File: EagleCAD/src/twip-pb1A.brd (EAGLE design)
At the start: 100 x 48.2 mm, 22 parts, among them J1 UJ2-BH-1-TH

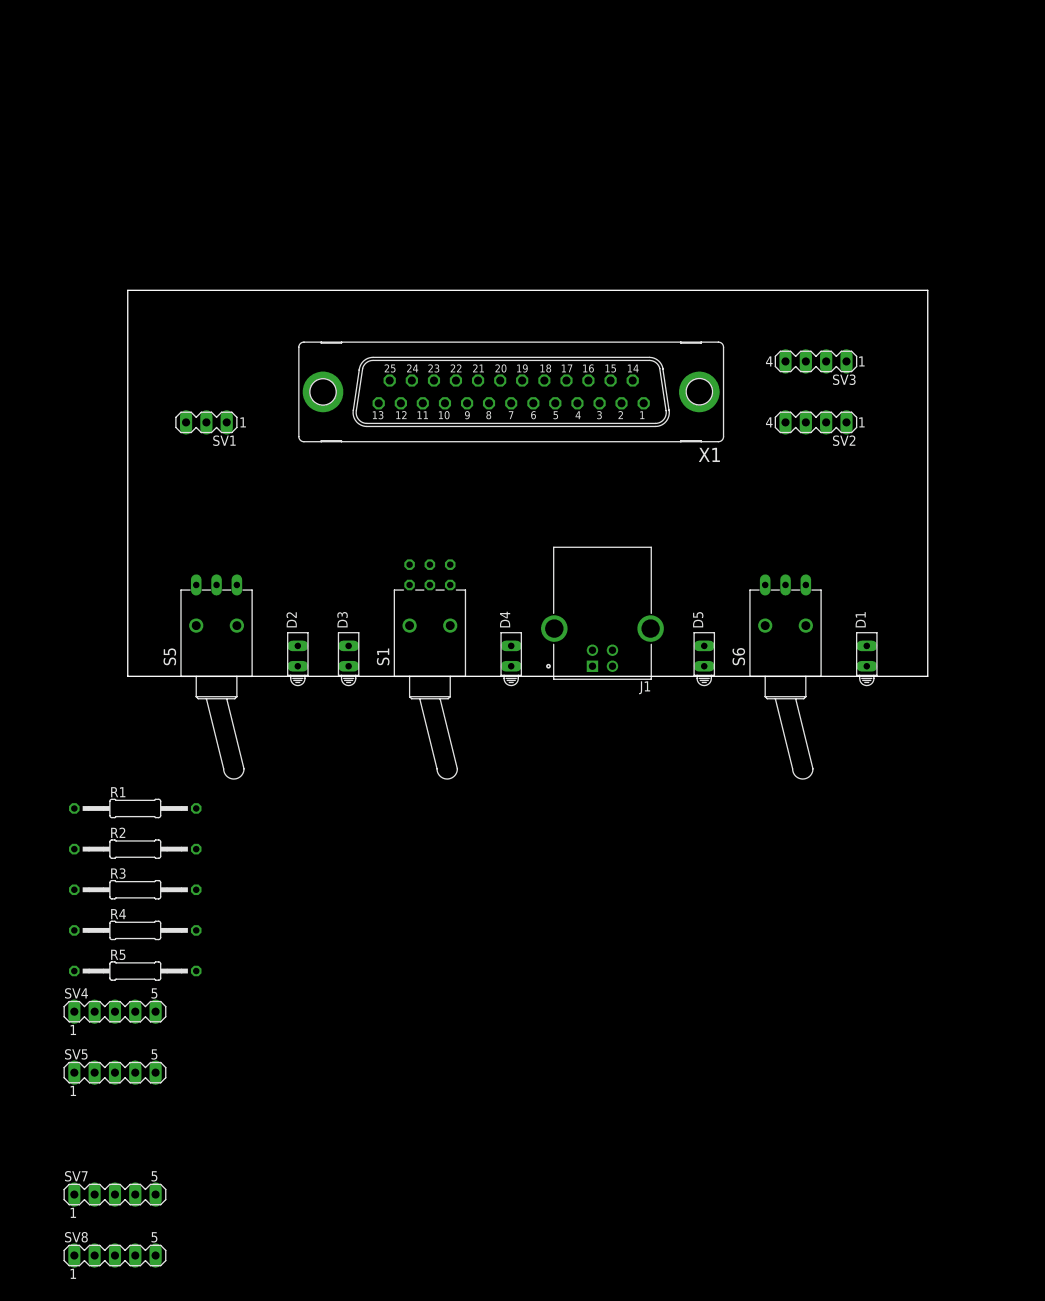
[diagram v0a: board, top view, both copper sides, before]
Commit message: Sep 24 checkpoint has mutually consistent versions of MB and PB layouts, and pinouts documentation
completed layout of peripheral board, with a few retrofits to MB for IBC connector changes. Added a 4 position DIP switch to PB as a way to have jumpers that cross other traces, as I couldn't quite do a single sided layout. All switches go to the right when active, and the voltage regulators, whose 4 legs are represented by two 5 pin headers, are correctly scaled. I'd like to space out the top connector for the stepper motor connections, but the board is at the max size allowed, and Eagle CAD won't allow it to be moved upward.
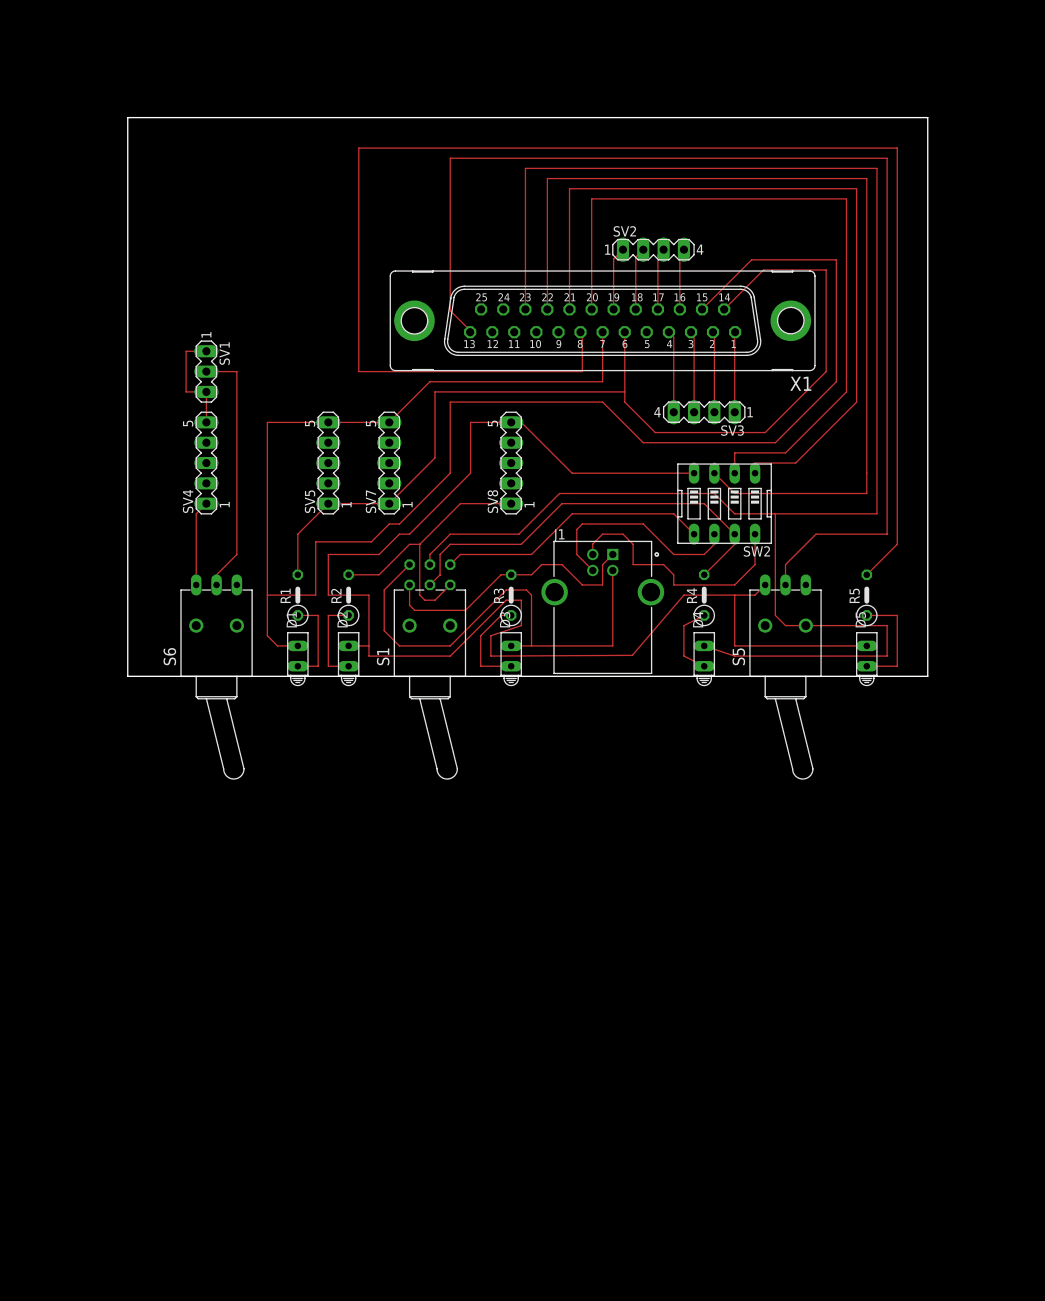
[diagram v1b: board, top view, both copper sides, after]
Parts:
- added SW2: (no value), special:EDG-04
- R1, R2, R3, R4, R5: device resistor:0207/15 -> resistor:0207/5V
- moved SV8 110.8 mm to (49.5, 58.4), turned to 90 degrees
- moved R5 102.8 mm to (94.0, 41.9), turned to 90 degrees
- moved SV7 97.7 mm to (34.3, 58.4), turned to 90 degrees
- moved R4 82.5 mm to (73.7, 41.9), turned to 90 degrees
- moved SV5 80.7 mm to (26.7, 58.4), turned to 90 degrees
- moved D1 71.1 mm to (22.9, 34.3)
- moved S5 71.1 mm to (83.8, 38.1)
- moved S6 71.1 mm to (12.7, 38.1)
- moved SV4 69.5 mm to (11.4, 58.4), turned to 90 degrees
- moved R3 59.7 mm to (49.5, 41.9), turned to 90 degrees
- moved R2 41.5 mm to (29.2, 41.9), turned to 90 degrees
- moved R1 33.5 mm to (22.9, 41.9), turned to 90 degrees
- moved SV2 29.6 mm to (67.3, 85.1), turned to 0 degrees
- moved D4 24.1 mm to (73.7, 34.3)
- moved D5 20.3 mm to (94.0, 34.3)
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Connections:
- new net N$22: R4.2, S1.2, SW2.7
- new net N$23: D3.K, J1.4, S1.6
- new net N$24: SW2.1, X1.21
- new net N$25: SW2.3, X1.22
- new net N$26: SW2.2, X1.20
- new net N$27: D4.K, S1.5, X1.23
- new net N$28: S5.2, X1.13
- new net N$29: D1.K, SV5.5, SV7.5, X1.15, X1.7
- new net N$30: S1.4, SW2.5
- new net N$31: D2.K, D5.K, S5.3, SV8.5, SW2.4
- new net N$33: J1.3, SW2.6
- net N$1: now also D1.A; no longer D2.A
- net N$10: now also S6.3; no longer S6.2
- net N$12: now also S1.1
- net N$13: now also J1.2, SW2.8; no longer D1.K, SV8.5
- net N$2: now also D2.A; no longer D1.A
- net N$7: now also S6.2; no longer S6.3
- net N$8: now also X1.14
- net N$9: now also J1.1, R3.2, S1.3; no longer D2.K, SV5.5, SV7.5, X1.5
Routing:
- net N$27: track 0.00 -> 220.2 mm
- net N$29: track 0.00 -> 211.3 mm
- net N$21: track 0.00 -> 183.1 mm
- net N$31: track 0.00 -> 172.0 mm
- net N$28: track 0.00 -> 141.2 mm
- net N$8: track 0.00 -> 124.3 mm
- net N$25: track 0.00 -> 115.8 mm
- net N$24: track 0.00 -> 94.8 mm
- net N$26: track 0.00 -> 89.7 mm
- net N$23: track 0.00 -> 60.4 mm
- net N$22: track 0.00 -> 52.1 mm
- net N$12: track 0.00 -> 35.2 mm
- net N$9: track 0.00 -> 34.7 mm
- net N$30: track 0.00 -> 34.2 mm
- net N$13: track 0.00 -> 31.8 mm
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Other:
- board size 100 x 48.2 mm -> 100 x 69.8 mm

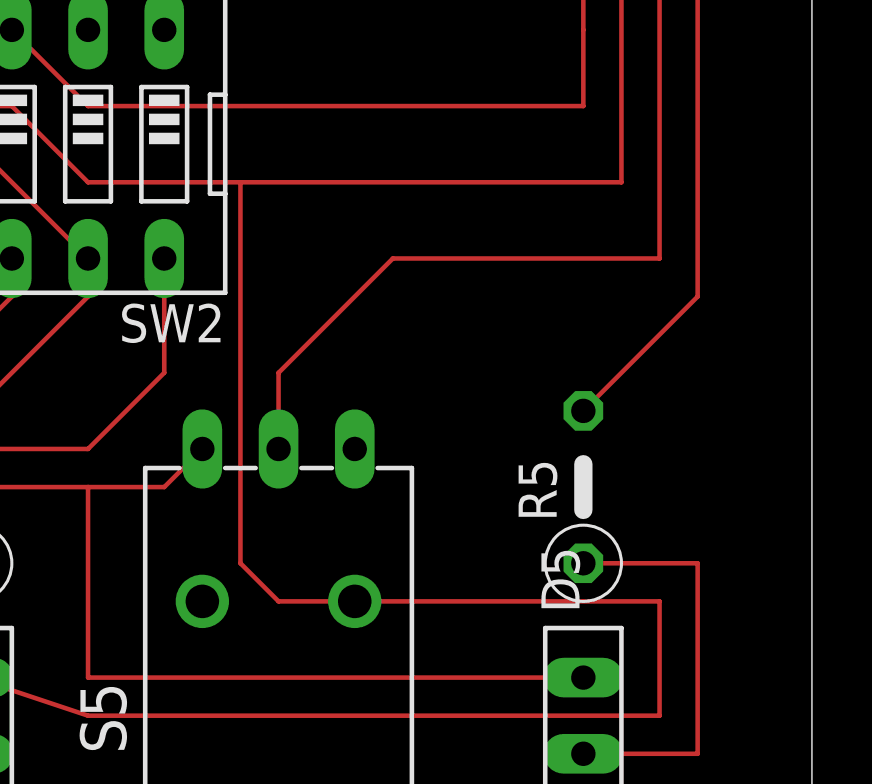
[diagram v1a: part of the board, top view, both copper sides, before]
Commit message: minor layout fixes
need to use version numbers built into copper plate.
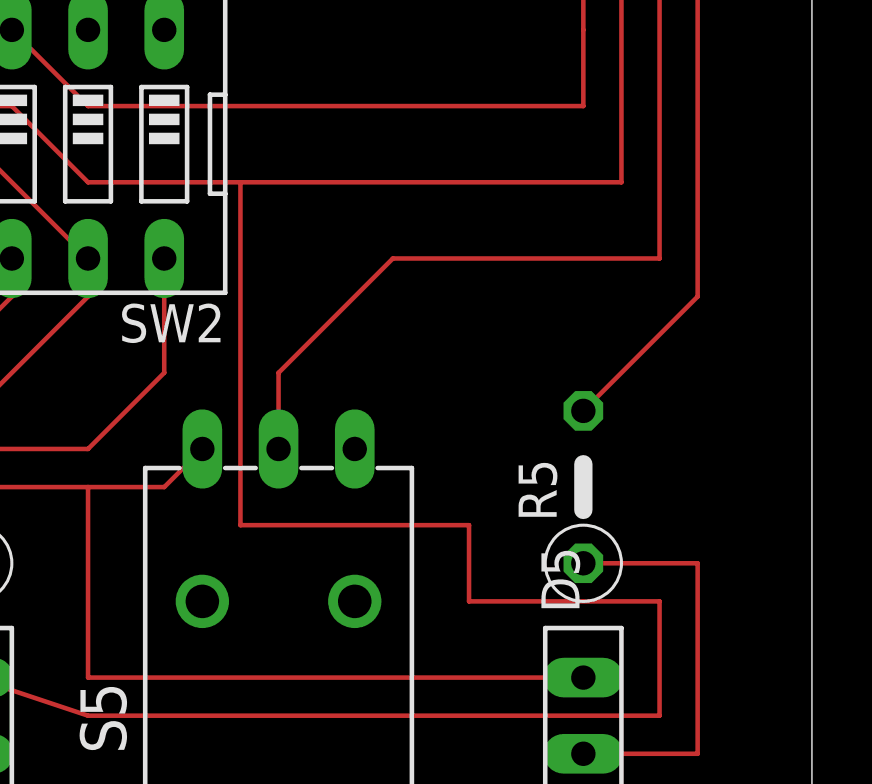
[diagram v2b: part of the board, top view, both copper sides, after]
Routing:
- net N$27: track 220.2 -> 220.9 mm
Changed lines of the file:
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@@
 <contactref element="D4" pad="K"/>
 <wire x1="55.5752" y1="54.61" x2="50.4952" y2="49.53" width="0.1524" layer="1"/>
-<wire x1="83.82" y1="38.1" x2="96.52" y2="38.1" width="0.1524" layer="1"/>
 <wire x1="96.52" y1="38.1" x2="96.52" y2="34.29" width="0.1524" layer="1"/>
 <wire x1="96.52" y1="34.29" x2="77.47" y2="34.29" width="0.1524" layer="1"/>
@@
 <wire x1="39.37" y1="45.72" x2="39.37" y2="46.99" width="0.1524" layer="1"/>
 <wire x1="41.91" y1="49.53" x2="50.4952" y2="49.53" width="0.1524" layer="1"/>
-<wire x1="82.55" y1="39.37" x2="83.82" y2="38.1" width="0.1524" layer="1"/>
 <wire x1="51.308" y1="95.25" x2="95.25" y2="95.25" width="0.1524" layer="1"/>
 <wire x1="95.25" y1="95.25" x2="95.25" y2="52.07" width="0.1524" layer="1"/>
@@
 <wire x1="77.47" y1="52.07" x2="74.93" y2="54.61" width="0.1524" layer="1"/>
 <wire x1="74.93" y1="54.61" x2="55.5752" y2="54.61" width="0.1524" layer="1"/>
-<wire x1="82.55" y1="39.37" x2="82.55" y2="52.07" width="0.1524" layer="1"/>
+<wire x1="82.55" y1="40.64" x2="82.55" y2="52.07" width="0.1524" layer="1"/>
 <wire x1="39.37" y1="46.99" x2="41.91" y2="49.53" width="0.1524" layer="1"/>
+<wire x1="82.55" y1="40.64" x2="90.17" y2="40.64" width="0.1524" layer="1"/>
+<wire x1="90.17" y1="40.64" x2="90.17" y2="38.1" width="0.1524" layer="1"/>
+<wire x1="90.17" y1="38.1" x2="96.52" y2="38.1" width="0.1524" layer="1"/>
 </signal>
 <signal name="N$28">

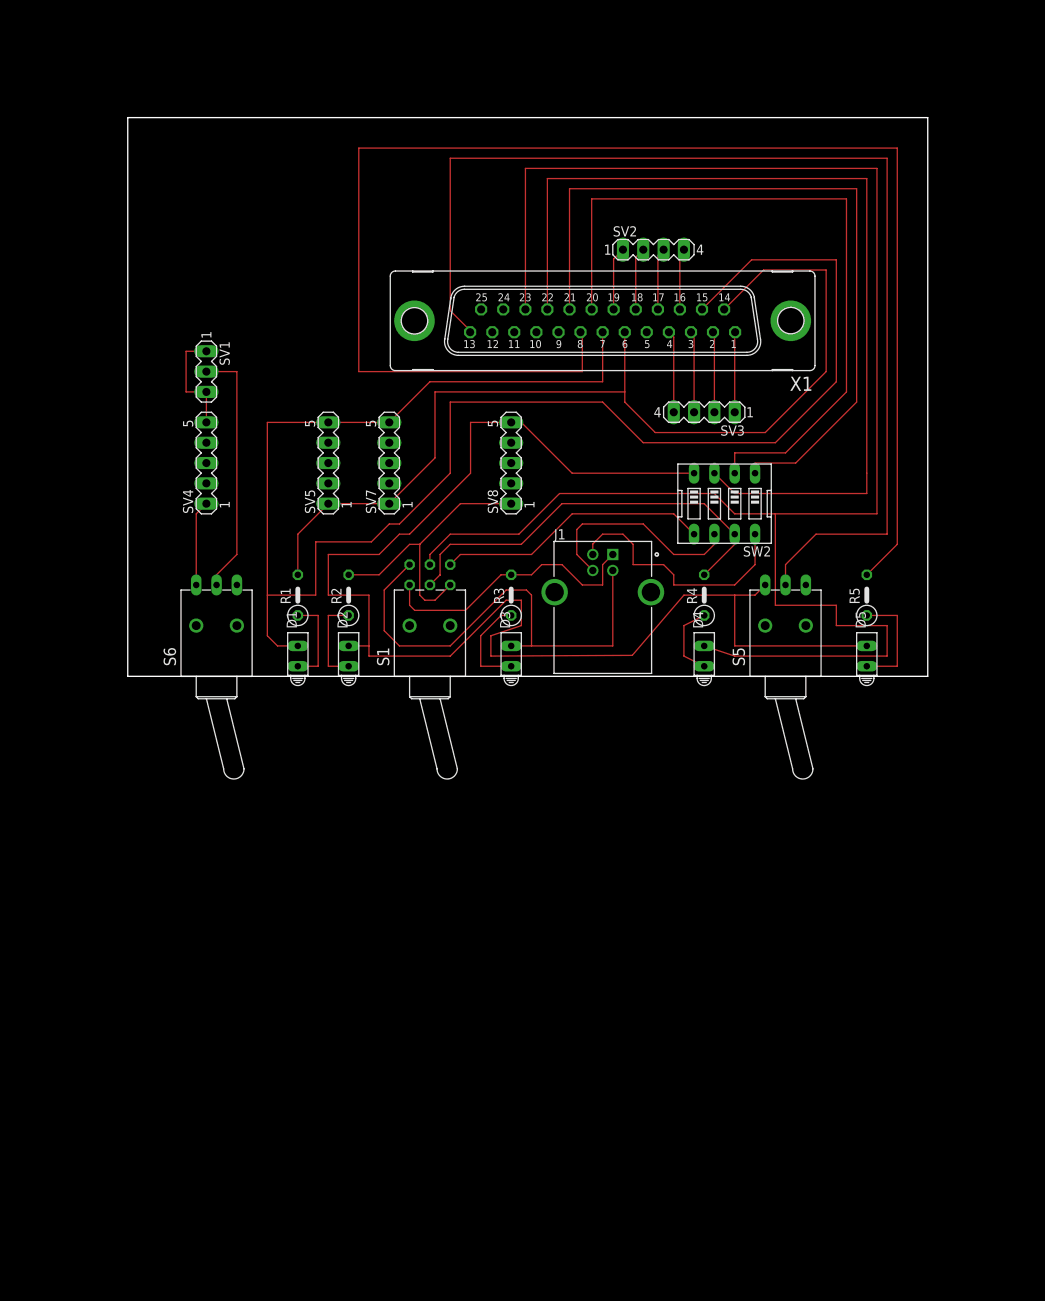
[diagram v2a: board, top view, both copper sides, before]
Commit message: minor fixes, and upsized boards to 3.3 x 5 inches
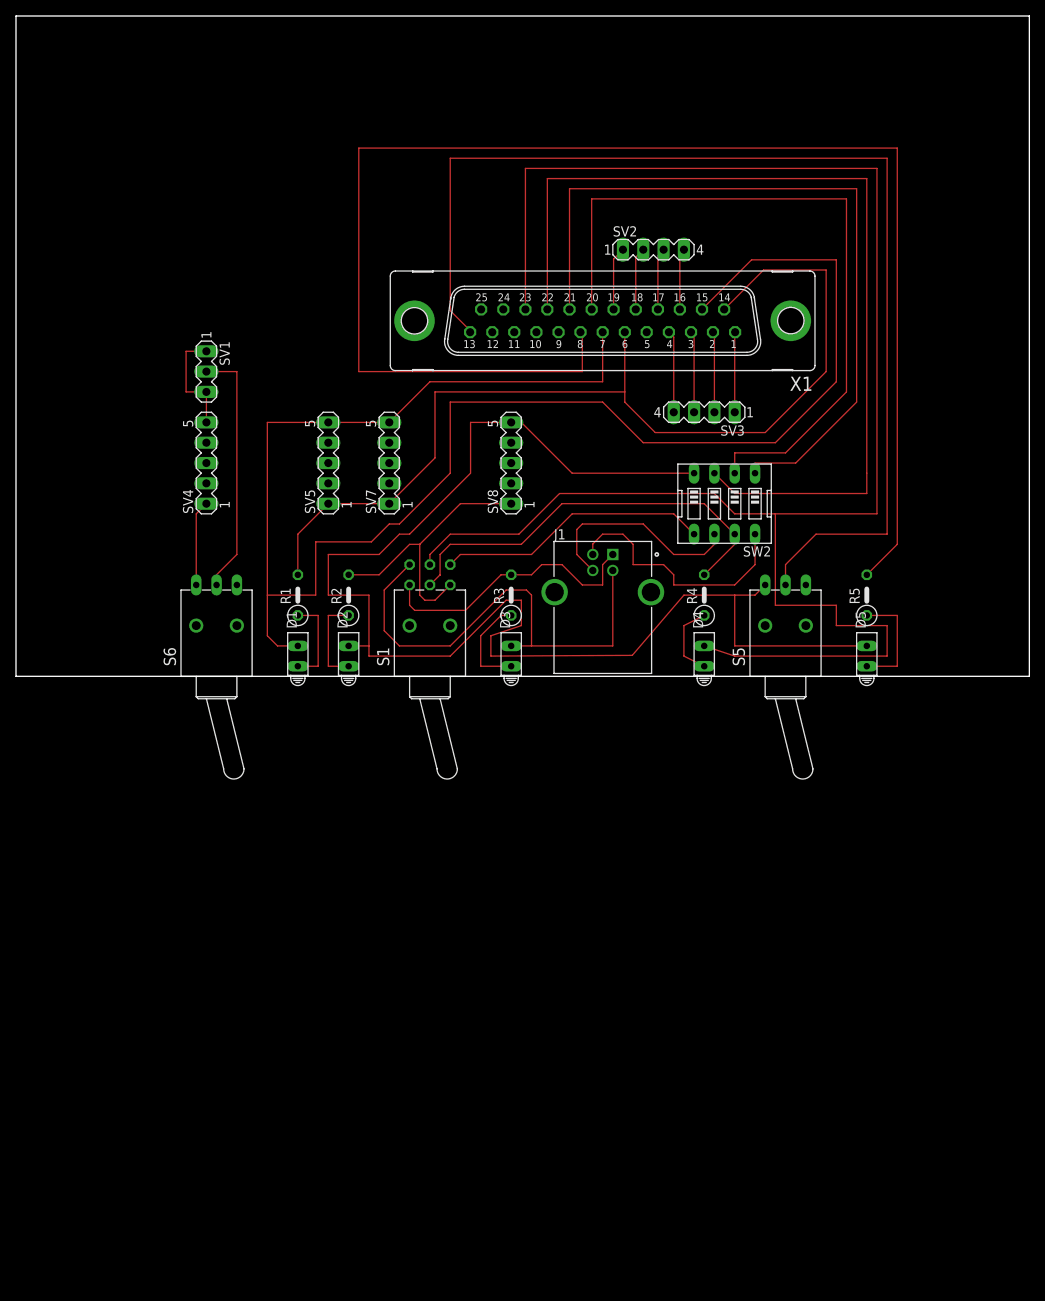
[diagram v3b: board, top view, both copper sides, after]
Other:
- board size 100 x 69.8 mm -> 126.7 x 82.5 mm
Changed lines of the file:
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@@
 <setting verticaltext="up"/>
 </settings>
-<grid distance="50" unitdist="mil" unit="mil" style="lines" multiple="1" display="no" altdistance="5" altunitdist="mil" altunit="mil"/>
+<grid distance="50" unitdist="mil" unit="mil" style="lines" multiple="10" display="yes" altdistance="5" altunitdist="mil" altunit="mil"/>
 <layers>
 <layer number="1" name="Top" color="4" fill="1" visible="yes" active="yes"/>
@@
 </layers>
 <board>
+<fusionsync huburn="a.cGVyc29uYWw6dWUyZDlmNmRl" projecturn="a.cGVyc29uYWw6dWUyZDlkNTAxIzIwMTgwODE4MTQ0NTE2MDUx" f3durn="urn:adsk.wipprod:dm.lineage:0yhwyiUNTZiQcmkfIzc17A" pcbguid="0e7eb315-b537-445a-a3fe-deb230e75ce0" lastpulledtime="" lastsyncedchangeguid="4e02391e-1938-e666-ed35-ac1e4dc4cf74"/>
 <plain>
-<wire x1="101.6" y1="101.6" x2="1.6" y2="101.6" width="0" layer="20"/>
-<wire x1="1.6" y1="101.6" x2="1.6" y2="31.76" width="0" layer="20"/>
-<wire x1="1.6" y1="31.76" x2="101.6" y2="31.76" width="0" layer="20"/>
-<wire x1="101.6" y1="31.76" x2="101.6" y2="101.6" width="0" layer="20"/>
-<dimension x1="101.6" y1="26.67" x2="2.54" y2="24.13" x3="52.07" y3="25.4" textsize="1.778" layer="1" dtype="horizontal" unit="inch"/>
-<dimension x1="-1.27" y1="31.75" x2="-1.27" y2="80.01" x3="-2.54" y3="55.88" textsize="1.778" layer="1" dtype="horizontal" unit="inch"/>
+<wire x1="114.3" y1="114.3" x2="-12.37" y2="114.3" width="0" layer="20"/>
+<wire x1="-12.37" y1="114.3" x2="-12.37" y2="31.76" width="0" layer="20"/>
+<wire x1="-12.37" y1="31.76" x2="114.3" y2="31.76" width="0" layer="20"/>
+<wire x1="114.3" y1="31.76" x2="114.3" y2="114.3" width="0" layer="20"/>
+<dimension x1="114.3" y1="120.65" x2="-12.7" y2="120.65" x3="50.8" y3="123.19" textsize="1.778" layer="1" extlength="1.27" unit="inch"/>
+<dimension x1="120.65" y1="114.3" x2="120.65" y2="30.48" x3="124.46" y3="72.39" textsize="1.778" layer="1" extlength="1.27" unit="inch"/>
 </plain>
 <attributes>
@@
 </note>
 <note version="8.3" severity="warning">
+Since Version 8.3, EAGLE supports Fusion synchronisation.
+This feature will not be available in this version and saving
+the document will break the link to the Fusion PCB feature.
+</note>
+<note version="8.3" severity="warning">
